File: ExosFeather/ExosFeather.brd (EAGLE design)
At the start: 50.8 x 22.9 mm, 21 parts, among them J1 JST_PH_2_PTH, J2 TC_2050_IDC_TOP, J6 CONN_2X1_JST_PA, U1 TVS_USB_TPD4S012, U2 STM32L052KX, U3 TI_CHGR_BQ21040

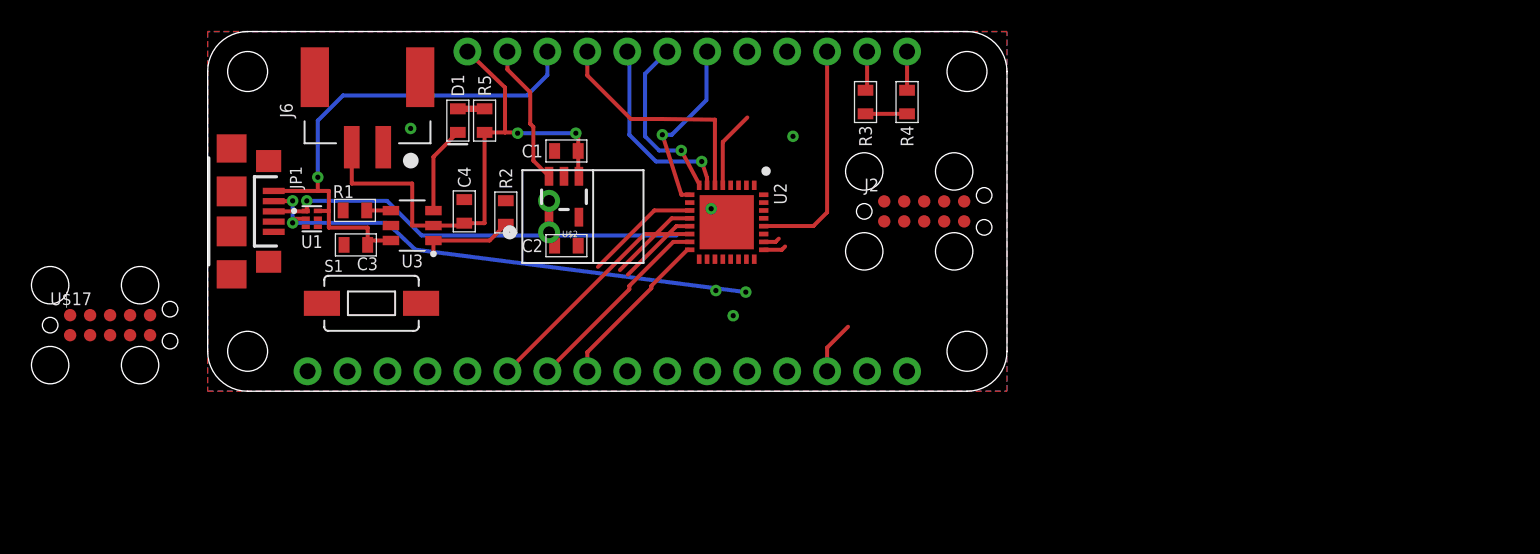
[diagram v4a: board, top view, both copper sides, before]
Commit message: updating exosFeather
need to:
1. add jumpers for enable pin & USB power routing
2. pin names
3. decide on PB1 & 2 &3
4. route enable pin
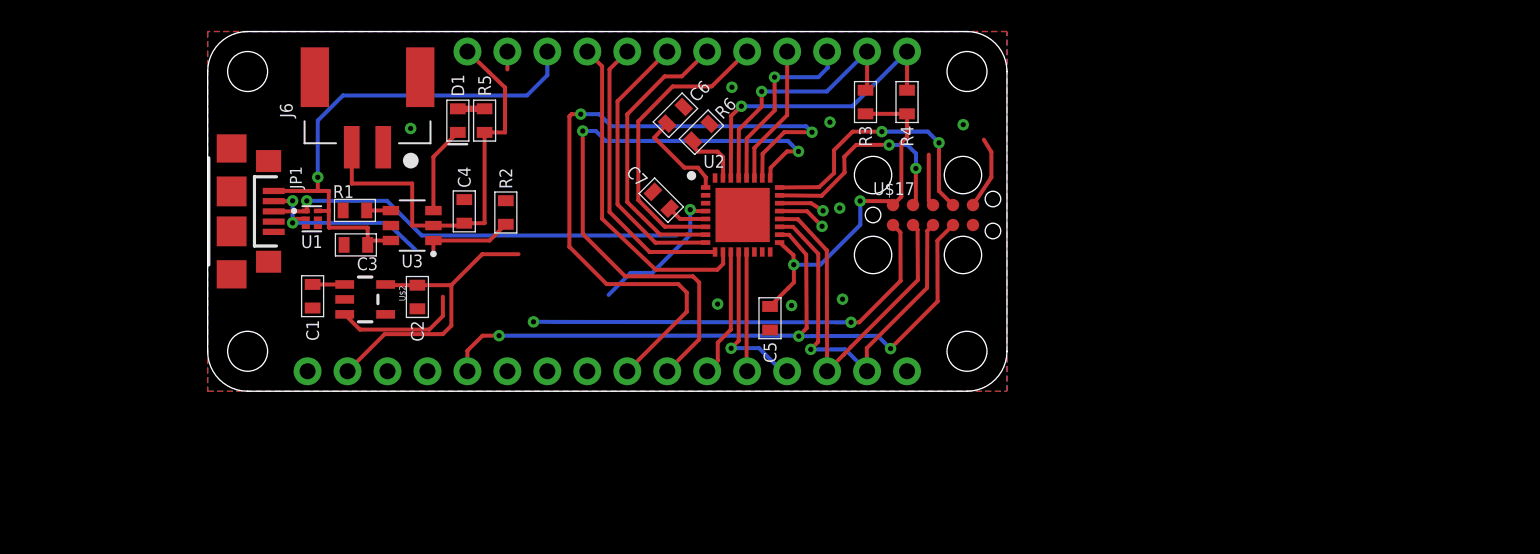
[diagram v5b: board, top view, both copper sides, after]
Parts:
- removed J1: JST_PH_2_PTH, stepOSP:JST_PH_PTH_2
- removed J2: TC_2050_IDC_TOP, leaf:TC_2050_IC_TOP
- removed S1: SWITCH-MOMENTARY-2-SMD-1101NE, SparkFun-Electromechanical:TACTILE-SWITCH-1101NE
- added C5, C6, C7, R6: (no value), stepOSP:0603
- moved U$17 52.8 mm to (46.1, 11.2)
- moved C1 18.6 mm to (6.67, 6.04), turned to 270 degrees
- moved U$2 14.2 mm to (10.0, 5.84), turned to 270 degrees
- moved C2 10.0 mm to (13.3, 5.99), turned to 270 degrees
- moved U2 1.11 mm to (34.0, 11.2), turned to 0 degrees
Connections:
- removed net N_RESET: J2.10
- new net N$1: R6.P$1, U2.31
- net +3V3: now also C5.P$1, C6.P$1, C7.P$1, U$17.10; no longer J2.1
- net CLK_IN: now also U$1.P$8; no longer U$1.P$4
- net DAC: now also U$1.P$4; no longer U$1.P$8
- net DE2: now also U$1.P$7; no longer U$1.P$5
- net GND: now also C5.P$2, C6.P$2, C7.P$2, R6.P$2, U$17.6, U$17.8; no longer J2.3, J2.5
- net MCO: now also U$17.4; no longer J2.7
- net N$3: no longer J1.P$2
- net NRST: now also U$17.1
- net RX1: now also U$17.2; no longer J2.9
- net RX2: now also U$1.P$5; no longer U$1.P$7
- net SWO: now also U$17.5; no longer J2.6
- net SW_CLK: now also U$17.7; no longer J2.4
- net SW_DIO: now also U$17.9; no longer J2.2
- net TX1: now also U$17.3; no longer J2.8
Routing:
- net MCO: track 0.00 -> 46.1 mm, vias 0 -> 3
- net +3V3: track 7.60 -> 51.3 mm, vias 0 -> 2
- net PB3: track 1.05 -> 44.7 mm, vias 0 -> 2
- net NRST: track 0.00 -> 37.6 mm, vias 0 -> 3
- net NSS: track 1.45 -> 38.8 mm, vias 0 -> 2
- net TX1: track 0.00 -> 24.7 mm, vias 0 -> 1
- net DAC: track 0.00 -> 20.9 mm
- net RX1: track 3.38 -> 23.3 mm
- net D-: track 33.5 -> 15.5 mm
- net SW_CLK: track 0.00 -> 17.0 mm, vias 0 -> 2
- net SDA: track 2.46 -> 19.3 mm, vias 0 -> 1
- net EVENT: track 15.2 -> 0.00 mm
- net SW_DIO: track 0.00 -> 14.2 mm, vias 0 -> 2
- net SCL: track 2.50 -> 16.3 mm, vias 0 -> 1
- net PB1: track 12.6 -> 0.00 mm
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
